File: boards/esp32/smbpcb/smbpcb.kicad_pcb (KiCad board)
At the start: 2 copper layers, 85.4 x 70.4 mm, 74 parts, among them IC1 MiCS-6814, J1 USB_B_Micro, J2 PMS7003, Q1 SUD08P06-155L, Q2 SS8050_NPN, Q3 SS8050_NPN, SW1 RESET, SW2 RESET, U1 MCP73831-2-OT, U2 TPS61200DRC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

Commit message: assembly QOL improvements
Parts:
- moved SW2 18.3 mm to (35.0, 56.0), turned to 90 degrees
- moved R25 6.25 mm to (44.5, 57.5), turned to 90 degrees
- moved R13 4.31 mm to (80.0, 81.2)
- moved R27 3.59 mm to (65.7, 76.7), turned to 90 degrees
- moved D1 2.78 mm to (43.8, 53.5), turned to 180 degrees
- moved R10 2.69 mm to (62.3, 56.6)
- moved R26 2.48 mm to (43.8, 67.1), turned to 90 degrees
- moved R2 2.31 mm to (63.2, 50.8)
- moved R28 1.99 mm to (42.2, 57.5), turned to 90 degrees
- moved C3 1.91 mm to (60.7, 49.1)
- moved SW1 1.89 mm to (54.0, 69.9)
- moved R18 1.78 mm to (100.4, 50.8)
- moved R17 1.76 mm to (100.4, 48.7)
- moved C6 1.60 mm to (99.8, 43.6)
- moved R3 1.60 mm to (63.2, 47.2), turned to 90 degrees
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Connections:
- D3 pad 1: Net-(C5-Pad1) -> GND
- D3 pad 2: Net-(D3-Pad2) -> Net-(R25-Pad2)
- R25 pad 1: Net-(D3-Pad2) -> +5V
- R25 pad 2: +5V -> Net-(R25-Pad2)
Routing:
- net GND: track 173.7 -> 186.4 mm, vias 19 -> 15
- net +3V3: track 213.1 -> 201.6 mm
- net Net-(C16-Pad2): track 6.29 -> 17.2 mm
- net Net-(Q2-Pad3): track 19.3 -> 12.8 mm
- net Net-(Q3-Pad2): track 12.7 -> 8.66 mm
- net Net-(C3-Pad1): track 23.6 -> 27.4 mm, vias 3 -> 2
- net Net-(C5-Pad1): track 6.09 -> 2.86 mm
- net Net-(J2-Pad5): track 15.1 -> 12.2 mm
- net +5V: track 38.0 -> 35.1 mm
- net NO2: track 22.7 -> 20.0 mm
- net Net-(R25-Pad2): track 0.00 -> 2.21 mm
- net Net-(D3-Pad2): track 1.99 -> 0.00 mm
- net EN: track 38.8 -> 40.5 mm
- net SCL: track 117.4 -> 119.0 mm
- net Net-(C6-Pad2): track 5.11 -> 3.49 mm
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
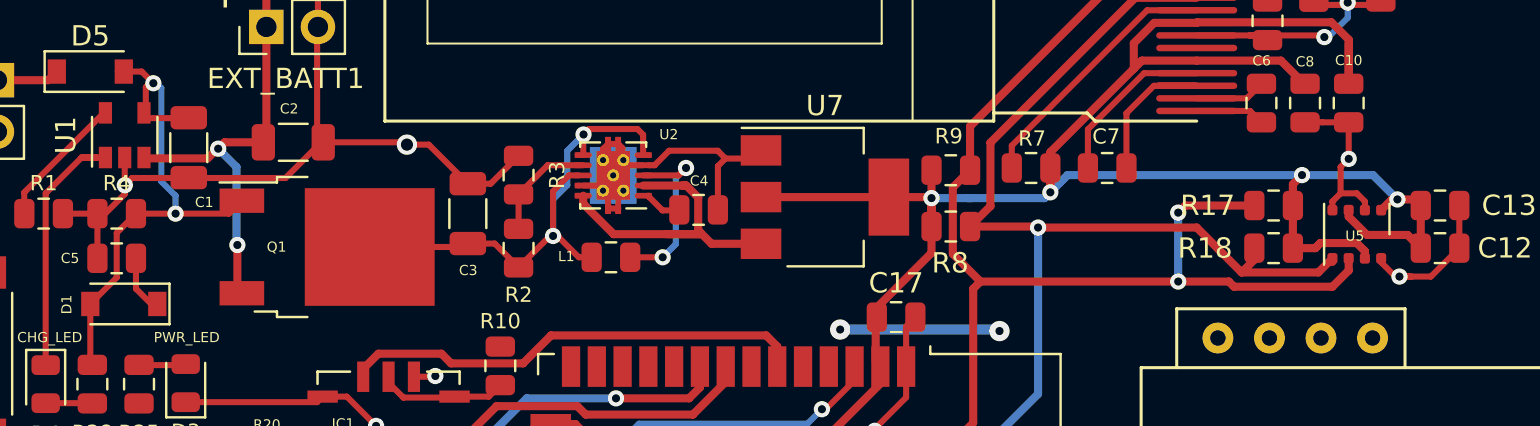
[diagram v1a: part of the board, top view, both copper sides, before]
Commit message: added dot for bme680
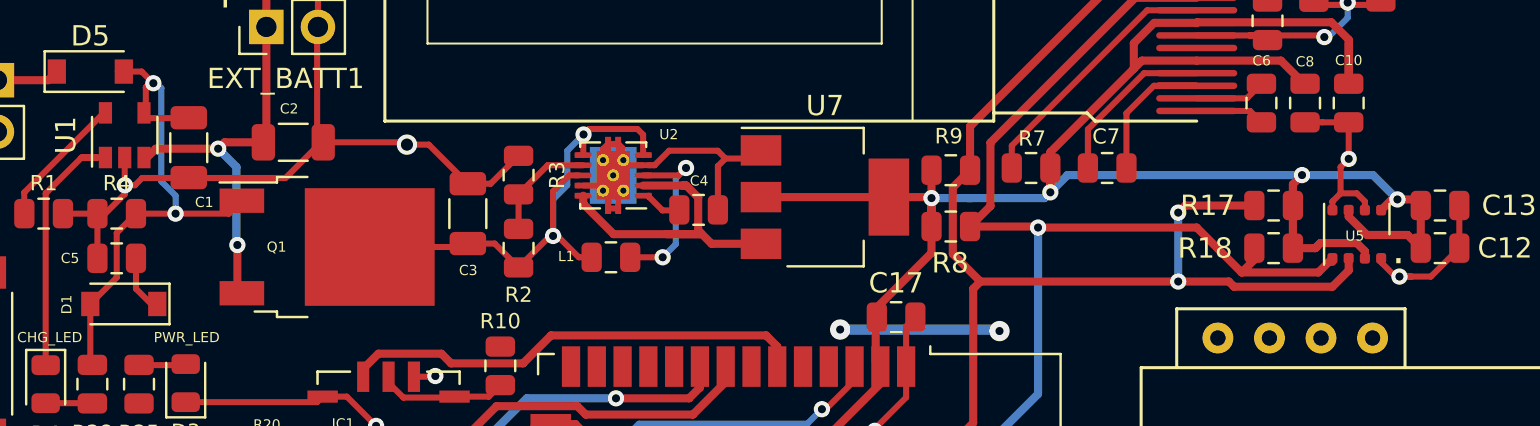
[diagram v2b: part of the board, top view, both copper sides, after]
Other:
- board text added: "."
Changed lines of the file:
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@@
     (fp_line (start -1.4 0.9) (end -1.4 -0.9) (layer "F.Fab") (width 0.1))
     (pad "1" smd rect (at -1.65 0) (locked) (size 0.9 1.2) (layers "F.Cu" "F.Paste" "F.Mask")
-      (net 64 "Net-(5V_IN1-Pad1)") (pinfunction "K") (pintype "passive"))
+      (net 64 "Net-(5V_IN1-Pad1)") (pinfunction "K"))
     (pad "2" smd rect (at 1.65 0) (locked) (size 0.9 1.2) (layers "F.Cu" "F.Paste" "F.Mask")
-      (net 76 "Net-(C1-Pad1)") (pinfunction "A") (pintype "passive"))
+      (net 76 "Net-(C1-Pad1)") (pinfunction "A"))
     (model "${KISYS3DMOD}/Diode_SMD.3dshapes/D_SOD-123.wrl"
       (offset (xyz 0 0 0))
@@
     (effects (font (size 1.5 1.5) (thickness 0.3)))
   )
+  (gr_text "." (at 106.55 50.85) (layer "F.SilkS")
+    (effects (font (size 1.5 1.5) (thickness 0.3)))
+  )
   (gr_text "IO0\n" (at 54.4 76.2) (layer "F.SilkS")
     (effects (font (size 1.5 1.5) (thickness 0.3)))
@@
   (segment (start 81.55 87.4) (end 80.95 86.8) (width 0.3) (layer "F.Cu") (net 1))
   (segment (start 54.738 58.115) (end 56.18 59.557) (width 0.3) (layer "F.Cu") (net 1))
+  (segment (start 46.9326 47.3444) (end 44.6556 47.3444) (width 0.3) (layer "F.Cu") (net 1))
   (segment (start 32.93 46.52) (end 32.93 45.92) (width 0.3) (layer "F.Cu") (net 1))
   (segment (start 53.275 39.94) (end 53.315 39.9) (width 0.3) (layer "F.Cu") (net 1))
-  (segment (start 46.9326 47.3444) (end 44.1556 47.3444) (width 0.3) (layer "F.Cu") (net 1))
   (segment (start 82.342 75.942) (end 82.342 75.94) (width 0.3) (layer "F.Cu") (net 1))
   (segment (start 73.01 46) (end 73.395 46.385) (width 0.3) (layer "F.Cu") (net 1))
+  (segment (start 44.3 47.7) (end 43.8 47.7) (width 0.3) (layer "F.Cu") (net 1))
   (segment (start 32.75 49.825) (end 30.7 47.775) (width 0.3) (layer "F.Cu") (net 1))
   (segment (start 30.7 45.325) (end 30.7 47.775) (width 0.3) (layer "F.Cu") (net 1))
@@
   (segment (start 66.3872 47.7156) (end 67.1122 47.7156) (width 0.3) (layer "F.Cu") (net 1))
   (segment (start 103.2983 48.5017) (end 103.2983 48.9274) (width 0.3) (layer "F.Cu") (net 1))
-  (segment (start 44.1556 47.3444) (end 43.8 47.7) (width 0.3) (layer "F.Cu") (net 1))
   (segment (start 69.90082 46.7156) (end 70.61642 46) (width 0.3) (layer "F.Cu") (net 1))
   (segment (start 62.6 66.85) (end 62.6 60.92638) (width 0.3) (layer "F.Cu") (net 1))
@@
   (segment (start 69.3372 46.7156) (end 68.6122 46.7156) (width 0.3) (layer "F.Cu") (net 1))
   (segment (start 103.7 48.1) (end 103.2983 48.5017) (width 0.3) (layer "F.Cu") (net 1))
+  (segment (start 44.6556 47.3444) (end 44.3 47.7) (width 0.3) (layer "F.Cu") (net 1))
   (segment (start 43.795 47.655) (end 43.795 46.335) (width 0.3) (layer "F.Cu") (net 1))
   (segment (start 68.6122 46.7156) (end 68.3622 46.4656) (width 0.3) (layer "F.Cu") (net 1))
@@
   (segment (start 42.1875 58.4375) (end 42.2 58.45) (width 0.3) (layer "F.Cu") (net 77))
   (segment (start 51.27 40.395) (end 50.775 39.9) (width 0.4) (layer "F.Cu") (net 78))
+  (segment (start 44.85162 46.3774) (end 45.32902 45.9) (width 0.4) (layer "F.Cu") (net 78))
   (segment (start 50.775 35.6025) (end 50.845 35.5325) (width 0.4) (layer "F.Cu") (net 78))
   (segment (start 48.715 45.585) (end 48.4 45.9) (width 0.4) (layer "F.Cu") (net 78))
-  (segment (start 48.35902 45.9) (end 47.88162 46.3774) (width 0.4) (layer "F.Cu") (net 78))
   (segment (start 50.325 45.585) (end 48.715 45.585) (width 0.4) (layer "F.Cu") (net 78))
-  (segment (start 44.85162 46.3774) (end 47.88162 46.3774) (width 0.4) (layer "F.Cu") (net 78))
+  (segment (start 48.35902 45.9) (end 48.4 45.9) (width 0.4) (layer "F.Cu") (net 78))
   (segment (start 49.3456 50.6446) (end 49.3456 52.7124) (width 0.4) (layer "F.Cu") (net 78))
+  (segment (start 45.32902 45.9) (end 48.35902 45.9) (width 0.4) (layer "F.Cu") (net 78))
   (segment (start 50.775 45.435) (end 50.625 45.585) (width 0.4) (layer "F.Cu") (net 78))
   (segment (start 50.775 39.9) (end 50.775 35.6025) (width 0.4) (layer "F.Cu") (net 78))
-  (segment (start 48.4 45.9) (end 48.35902 45.9) (width 0.4) (layer "F.Cu") (net 78))
   (segment (start 50.775 39.9) (end 50.775 45.435) (width 0.4) (layer "F.Cu") (net 78))
   (via (at 49.3456 50.6446) (size 0.8) (drill 0.4) (layers "F.Cu" "B.Cu") (net 78))

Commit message: these probbaly should have been 1 commit
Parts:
- moved R23 9.68 mm to (38.7, 84.3), turned to 90 degrees
- moved R22 6.64 mm to (41.0, 84.3), turned to 90 degrees
- moved L1 2.25 mm to (65.5, 51.2), turned to -90 degrees
- moved C14 2.11 mm to (104.2, 39.2)
- moved R17 1.88 mm to (101.6, 50.1), turned to 90 degrees
- moved C13 1.78 mm to (109.7, 50.1), turned to 90 degrees
- moved C11 1.54 mm to (102.0, 39.2)
- moved C4 1.43 mm to (72.3, 47.5), turned to 90 degrees
- moved C12 1.39 mm to (107.4, 50.1), turned to -90 degrees
- moved R18 1.28 mm to (99.3, 50.1), turned to 90 degrees
- moved R21 0.50 mm to (99.8, 39.2)
- moved R2 0.40 mm to (63.2, 51.2)
- moved R9 0.06 mm to (84.5, 46.9)
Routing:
- net Net-(J2-Pad5): track 12.2 -> 5.46 mm
- net SDA: track 131.1 -> 124.6 mm, vias 2 -> 1
- net Net-(C3-Pad1): track 27.4 -> 23.3 mm
- net +3V3: track 201.6 -> 197.8 mm, vias 6 -> 7
- net Net-(J2-Pad10): track 5.25 -> 2.47 mm
- net GND: track 186.4 -> 188.7 mm, vias 15 -> 12
- net Net-(C4-Pad1): track 1.80 -> 3.10 mm
- net SCL: track 119.0 -> 117.8 mm
- net Net-(C14-Pad2): track 9.49 -> 8.59 mm
- net +5V: track 35.1 -> 34.4 mm
- net ESP_RX2: track 41.1 -> 40.4 mm, vias 2 -> 1
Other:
- board text added: "TP_3v3_IN"
- board text added: "TP_SCL"
- board text added: "TP_SDA"

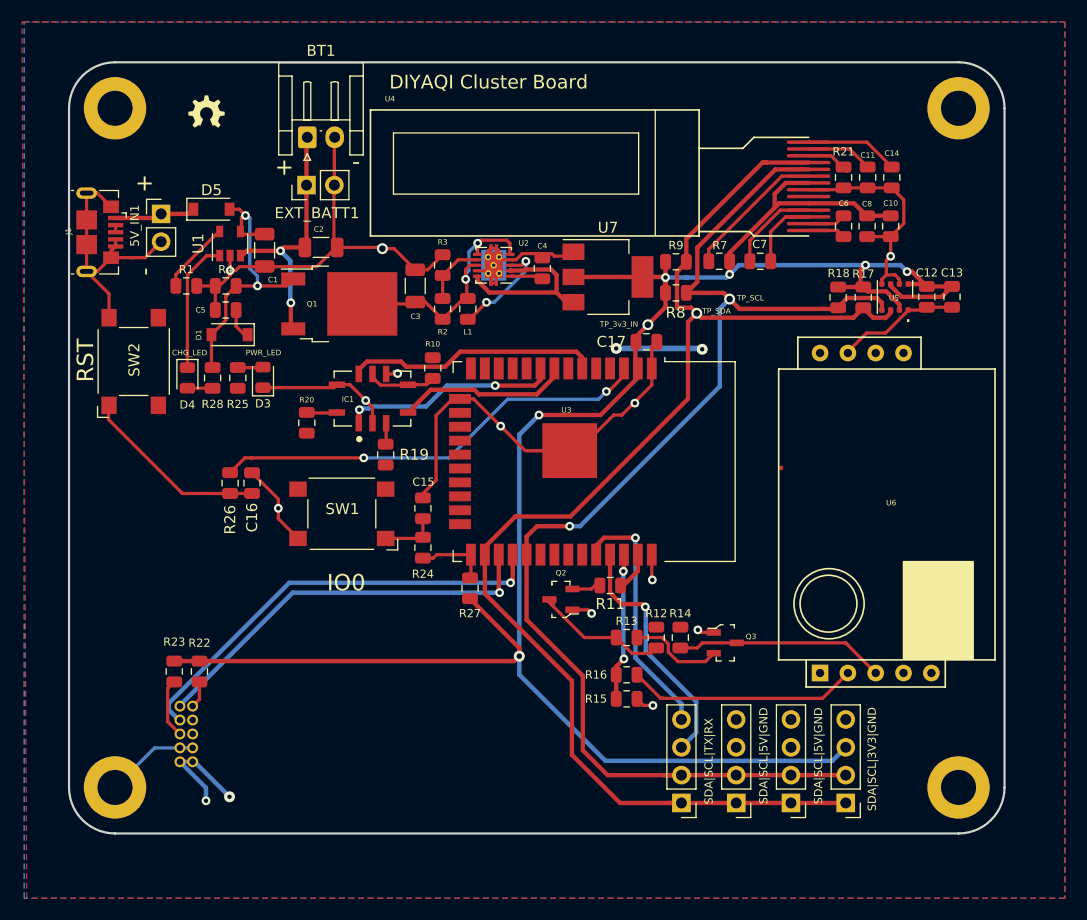
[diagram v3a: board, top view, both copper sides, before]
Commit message: wrong micro usb footprint
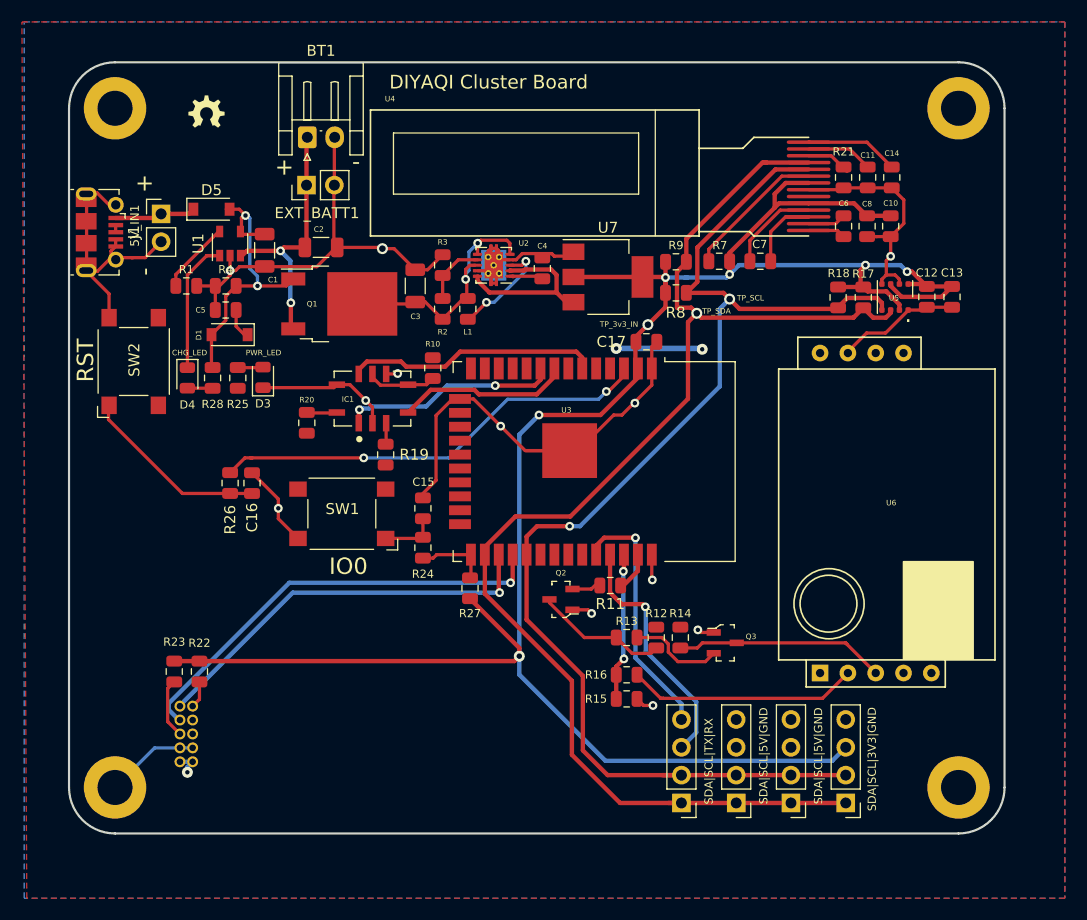
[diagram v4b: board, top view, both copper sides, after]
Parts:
- J1: footprint Connector_USB:USB_Micro-B_GCT_USB3076-30-A -> Connector_USB:USB_Micro-B_Molex-105017-0001
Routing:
- net +5V: track 34.4 -> 26.3 mm, vias 4 -> 3
- net Net-(Q2-Pad3): track 12.8 -> 12.2 mm

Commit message: v1 probably
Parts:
- removed C11, C14: 10uF, Capacitor_SMD:C_0805_2012Metric
- removed R21: 330k, Capacitor_SMD:C_0805_2012Metric
- removed R7, R8, R9: 10k, Capacitor_SMD:C_0805_2012Metric
- added C9: 10uF, Capacitor_SMD:C_0805_2012Metric, F.Cu at (102.0, 39.2)
- added R5: 10k, Capacitor_SMD:C_0805_2012Metric, F.Cu at (84.5, 46.8)
- added R6: 330k, Capacitor_SMD:C_0805_2012Metric, F.Cu at (99.8, 39.2)
- C10: value 1uF -> 10uF
- C3: value 4.7uF -> 10uF
- C4: value 1uF -> 10uF; footprint Capacitor_SMD:C_0805_2012Metric -> Capacitor_SMD:C_1206_3216Metric
- C5: value 22uF -> 1uF
- L1: value 2.2uH -> 4.7uH
- R2: value 2M -> 10k
- R3: value 180k -> 10k
- U2: value TPS61200DRC -> SGM6603-5.0YN6G_TR; footprint Package_SON:Texas_S-PVSON-N10_ThermalVias -> Package_TO_SOT_SMD:SOT-23-6
- moved C5 57.0 mm to (99.9, 43.6), turned to 90 degrees
- moved R2 25.7 mm to (88.5, 46.7), turned to 180 degrees
- moved R3 21.6 mm to (84.6, 49.8), turned to 0 degrees
- moved C7 12.5 mm to (104.3, 43.6), turned to -90 degrees
- moved C6 8.19 mm to (92.2, 46.7), turned to 0 degrees
- moved C10 4.45 mm to (104.2, 39.2), turned to 90 degrees
- moved L1 4.10 mm to (65.4, 47.1), turned to 90 degrees
- moved D1 2.05 mm to (43.7, 51.5)
- moved U2 0.80 mm to (68.5, 47.7), turned to -90 degrees
- moved Q3 0.74 mm to (88.8, 82.4)
- moved C4 0.41 mm to (71.9, 47.4)
- moved C8 0.16 mm to (102.1, 43.6)
- turned R17 to -90 degrees
- turned R18 to -90 degrees
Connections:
- C10 pad 1: +3V3 -> GND
- C10 pad 2: GND -> +3V3
- C4 pad 1: Net-(C4-Pad1) -> +5V
- C5 pad 1: Net-(C5-Pad1) -> Net-(U4-Pad1)
- C5 pad 2: GND -> Net-(U4-Pad2)
- C6 pad 1: Net-(C6-Pad1) -> Net-(U4-Pad4)
- C6 pad 2: Net-(C6-Pad2) -> Net-(U4-Pad3)
- C7 pad 1: Net-(C7-Pad1) -> +3V3
- C7 pad 2: Net-(C7-Pad2) -> GND
- D1 pad 1: Net-(C5-Pad1) -> +5V
- R17 pad 1: SDA -> +3V3
- R17 pad 2: +3V3 -> SDA
- R18 pad 1: SCL -> +3V3
- R18 pad 2: +3V3 -> SCL
- R2 pad 1: Net-(C3-Pad1) -> +3V3
- R2 pad 2: Net-(R2-Pad2) -> RES
- R3 pad 1: Net-(R2-Pad2) -> +3V3
- R3 pad 2: GND -> SCL
- U2 pad 1: Net-(C4-Pad1) -> Net-(L1-Pad2)
- U2 pad 2: +5V -> GND
- U2 pad 3: Net-(L1-Pad2) -> Net-(C3-Pad1)
- U2 pad 4: GND -> unconnected-(U2-Pad4)
- U2 pad 5: Net-(C3-Pad1) -> +5V
- U4 pad 1: Net-(C6-Pad1) -> Net-(U4-Pad1)
- U4 pad 14: Net-(C14-Pad2) -> +3V3
- U4 pad 2: Net-(C6-Pad2) -> Net-(U4-Pad2)
- U4 pad 3: Net-(C7-Pad1) -> Net-(U4-Pad3)
- U4 pad 4: Net-(C7-Pad2) -> Net-(U4-Pad4)
- U4 pad 9: Net-(R7-Pad2) -> RES
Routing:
- net +3V3: track 197.8 -> 220.5 mm
- net +5V: track 26.3 -> 13.1 mm, vias 3 -> 2
- net RES: track 0.00 -> 13.0 mm
- net Net-(R7-Pad2): track 13.0 -> 0.00 mm
- net Net-(U4-Pad3): track 0.00 -> 10.5 mm
- net Net-(C7-Pad1): track 10.5 -> 0.00 mm
- net Net-(C14-Pad2): track 8.59 -> 0.00 mm
- net Net-(U4-Pad4): track 0.00 -> 8.41 mm
- net Net-(C7-Pad2): track 8.41 -> 0.00 mm
- net GND: track 188.7 -> 181.9 mm, vias 12 -> 13
- net Net-(R2-Pad2): track 5.48 -> 0.00 mm
- net Net-(C3-Pad1): track 23.3 -> 18.0 mm, vias 2 -> 0
- net Net-(L1-Pad2): track 9.15 -> 4.91 mm, vias 2 -> 0
- net Net-(U4-Pad2): track 0.00 -> 3.61 mm
- net Net-(U4-Pad1): track 0.00 -> 3.50 mm
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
